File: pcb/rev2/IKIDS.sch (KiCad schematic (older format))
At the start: 41 parts, among them SW1 SW_Push, U1 ATmega32U4-AU, Y1 16MHz

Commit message: Added finished PCB to repo
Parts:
- removed F1: 500mA, Fuse:Fuse_1206_3216Metric, symbol Device:Polyfuse
- removed USB1: Molex-0548190519, random-keyboard-parts:Molex-0548190589, symbol random-keyboard-parts:Molex-0548190519
- removed USB?: HRO-TYPE-C-31-M-12, symbol keebio:HRO-TYPE-C-31-M-12
- added F1: 500mA, Fuse:Fuse_1206_3216Metric, symbol Device:Polyfuse_Small
- added USB1: Molex-0548190589, random-keyboard-parts:Molex-0548190589, symbol random-keyboard-parts:Molex-0548190589
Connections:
- net +5V: now also F1.1
- net D+: now also USB1.3 (D+)
- net D-: now also USB1.4 (D-)
- net GND: now also USB1.1 (GND)
- net VCC: now also F1.2, USB1.5 (VBUS)
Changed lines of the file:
@@
 Comment4 ""
 $EndDescr
-$Comp
-L MCU_Microchip_ATmega:ATmega32U4-AU U1
-U 1 1 607794AF
-P 9540 3080
-F 0 "U1" H 9540 1191 50  0000 C CNN
-F 1 "ATmega32U4-AU" H 9540 1100 50  0000 C CNN
-F 2 "Package_QFP:TQFP-44_10x10mm_P0.8mm" H 9540 3080 50  0001 C CIN
-F 3 "http://ww1.microchip.com/downloads/en/DeviceDoc/Atmel-7766-8-bit-AVR-ATmega16U4-32U4_Datasheet.pdf" H 9540 3080 50  0001 C CNN
-	1    9540 3080
-	1    0    0    -1
-$EndComp
-Wire Wire Line
-	9440 1280 9540 1280
-Connection ~ 9540 1280
-Wire Wire Line
-	9540 1280 9640 1280
 Wire Wire Line
 	9440 1280 9440 1180
-Connection ~ 9440 1280
 $Comp
 L power:+5V #PWR0101
@@
 	1    0    0    -1
 $EndComp
-Wire Wire Line
-	9540 4880 9440 4880
-Connection ~ 9440 4880
-Wire Wire Line
-	9440 4880 9340 4880
 $Comp
 L power:GND #PWR0102
@@
 	1    0    0    -1
 $EndComp
-$Comp
-L random-keyboard-parts:Molex-0548190519 USB1
-U 1 1 6077A7AA
-P 9290 5710
-F 0 "USB1" V 9827 5677 60  0000 C CNN
-F 1 "Molex-0548190519" V 9721 5677 60  0000 C CNN
-F 2 "random-keyboard-parts:Molex-0548190589" H 9290 5710 60  0001 C CNN
-F 3 "" H 9290 5710 60  0001 C CNN
-	1    9290 5710
-	0    -1   -1   0
-$EndComp
-Wire Wire Line
-	9590 5510 9790 5510
-$Comp
-L power:VCC #PWR0111
-U 1 1 6077D28D
-P 9790 5510
-F 0 "#PWR0111" H 9790 5360 50  0001 C CNN
-F 1 "VCC" H 9805 5683 50  0000 C CNN
-F 2 "" H 9790 5510 50  0001 C CNN
-F 3 "" H 9790 5510 50  0001 C CNN
-	1    9790 5510
-	1    0    0    -1
-$EndComp
-Wire Wire Line
-	9790 5510 9990 5510
-Connection ~ 9790 5510
-$Comp
-L Device:Polyfuse F1
-U 1 1 6077E43E
-P 10140 5510
-F 0 "F1" V 9915 5510 50  0000 C CNN
-F 1 "500mA" V 10006 5510 50  0000 C CNN
-F 2 "Fuse:Fuse_1206_3216Metric" H 10190 5310 50  0001 L CNN
-F 3 "~" H 10140 5510 50  0001 C CNN
-	1    10140 5510
-	0    1    1    0
-$EndComp
-Wire Wire Line
-	10290 5510 10390 5510
-$Comp
-L power:+5V #PWR0112
-U 1 1 6077F79A
-P 10390 5510
-F 0 "#PWR0112" H 10390 5360 50  0001 C CNN
-F 1 "+5V" H 10405 5683 50  0000 C CNN
-F 2 "" H 10390 5510 50  0001 C CNN
-F 3 "" H 10390 5510 50  0001 C CNN
-	1    10390 5510
-	1    0    0    -1
-$EndComp
-Text GLabel 9590 5610 2    50   Input ~ 0
-D-
-Text GLabel 9590 5710 2    50   Input ~ 0
-D+
 $Comp
 L MX_Alps_Hybrid:MX-LED MX3
@@
 Text GLabel 3950 3570 3    50   Input ~ 0
 led8
-$Comp
-L keebio:HRO-TYPE-C-31-M-12 USB?
-U 1 1 607E2252
-P 7470 5430
-F 0 "USB?" H 7303 6227 60  0000 C CNN
-F 1 "HRO-TYPE-C-31-M-12" H 7303 6121 60  0000 C CNN
-F 2 "" H 7470 5430 60  0001 C CNN
-F 3 "" H 7470 5430 60  0001 C CNN
-	1    7470 5430
-	1    0    0    -1
-$EndComp
-Wire Wire Line
-	7570 4980 7670 4980
-$Comp
-L power:+5V #PWR?
-U 1 1 607E72D0
-P 7670 4980
-F 0 "#PWR?" H 7670 4830 50  0001 C CNN
-F 1 "+5V" H 7685 5153 50  0000 C CNN
-F 2 "" H 7670 4980 50  0001 C CNN
-F 3 "" H 7670 4980 50  0001 C CNN
-	1    7670 4980
-	1    0    0    -1
-$EndComp
-Wire Wire Line
-	7570 5880 7670 5880
-$Comp
-L power:+5V #PWR?
-U 1 1 607EA54B
-P 7670 5880
-F 0 "#PWR?" H 7670 5730 50  0001 C CNN
-F 1 "+5V" H 7685 6053 50  0000 C CNN
-F 2 "" H 7670 5880 50  0001 C CNN
-F 3 "" H 7670 5880 50  0001 C CNN
-	1    7670 5880
-	1    0    0    -1
-$EndComp
-Wire Wire Line
-	7570 5980 7670 5980
-$Comp
-L power:GND #PWR?
-U 1 1 607EE216
-P 7670 5980
-F 0 "#PWR?" H 7670 5730 50  0001 C CNN
-F 1 "GND" H 7675 5807 50  0000 C CNN
-F 2 "" H 7670 5980 50  0001 C CNN
-F 3 "" H 7670 5980 50  0001 C CNN
-	1    7670 5980
-	1    0    0    -1
-$EndComp
+Connection ~ 9440 4880
+Wire Wire Line
+	9440 4880 9340 4880
+Wire Wire Line
+	9540 4880 9440 4880
+Connection ~ 9440 1280
+Connection ~ 9540 1280
+Wire Wire Line
+	9540 1280 9640 1280
+Wire Wire Line
+	9440 1280 9540 1280
+$Comp
+L MCU_Microchip_ATmega:ATmega32U4-AU U1
+U 1 1 607794AF
+P 9540 3080
+F 0 "U1" H 9540 1191 50  0000 C CNN
+F 1 "ATmega32U4-AU" H 9540 1100 50  0000 C CNN
+F 2 "Package_QFP:TQFP-44_10x10mm_P0.8mm" H 9540 3080 50  0001 C CIN
+F 3 "http://ww1.microchip.com/downloads/en/DeviceDoc/Atmel-7766-8-bit-AVR-ATmega16U4-32U4_Datasheet.pdf" H 9540 3080 50  0001 C CNN
+	1    9540 3080
+	1    0    0    -1
+$EndComp
+$Comp
+L random-keyboard-parts:Molex-0548190589 USB1
+U 1 1 6079F11B
+P 1670 6340
+F 0 "USB1" V 2207 6307 60  0000 C CNN
+F 1 "Molex-0548190589" V 2101 6307 60  0000 C CNN
+F 2 "random-keyboard-parts:Molex-0548190589" H 1670 6340 60  0001 C CNN
+F 3 "" H 1670 6340 60  0001 C CNN
+	1    1670 6340
+	0    -1   -1   0
+$EndComp
+Wire Wire Line
+	1970 6140 2170 6140
+$Comp
+L power:VCC #PWR0111
+U 1 1 607A247B
+P 2170 6140
+F 0 "#PWR0111" H 2170 5990 50  0001 C CNN
+F 1 "VCC" H 2185 6313 50  0000 C CNN
+F 2 "" H 2170 6140 50  0001 C CNN
+F 3 "" H 2170 6140 50  0001 C CNN
+	1    2170 6140
+	1    0    0    -1
+$EndComp
+Wire Wire Line
+	2170 6140 2320 6140
+Connection ~ 2170 6140
+$Comp
+L Device:Polyfuse_Small F1
+U 1 1 607A5C52
+P 2420 6140
+F 0 "F1" V 2215 6140 50  0000 C CNN
+F 1 "500mA" V 2306 6140 50  0000 C CNN
+F 2 "Fuse:Fuse_1206_3216Metric" H 2470 5940 50  0001 L CNN
+F 3 "~" H 2420 6140 50  0001 C CNN
+	1    2420 6140
+	0    1    1    0
+$EndComp
+Wire Wire Line
+	2520 6140 2720 6140
+$Comp
+L power:+5V #PWR0112
+U 1 1 607A8D6A
+P 2720 6140
+F 0 "#PWR0112" H 2720 5990 50  0001 C CNN
+F 1 "+5V" H 2735 6313 50  0000 C CNN
+F 2 "" H 2720 6140 50  0001 C CNN
+F 3 "" H 2720 6140 50  0001 C CNN
+	1    2720 6140
+	1    0    0    -1
+$EndComp
+$Comp
+L power:GND #PWR0122
+U 1 1 607A956C
+P 1970 6540
+F 0 "#PWR0122" H 1970 6290 50  0001 C CNN
+F 1 "GND" H 1975 6367 50  0000 C CNN
+F 2 "" H 1970 6540 50  0001 C CNN
+F 3 "" H 1970 6540 50  0001 C CNN
+	1    1970 6540
+	1    0    0    -1
+$EndComp
+Text GLabel 1970 6240 2    50   Input ~ 0
+D-
+Text GLabel 1970 6340 2    50   Input ~ 0
+D+
 $EndSCHEMATC

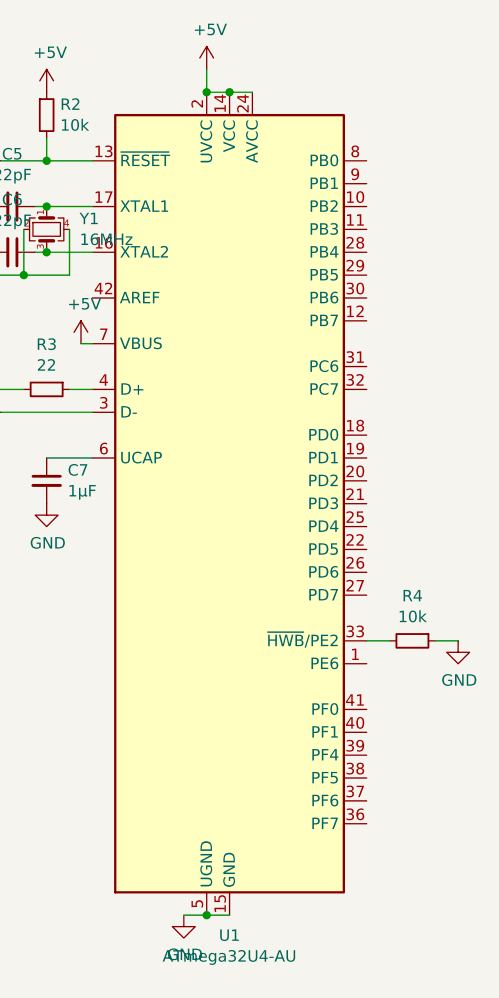
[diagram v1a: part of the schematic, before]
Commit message: added PCB files that doesn't require elite-c
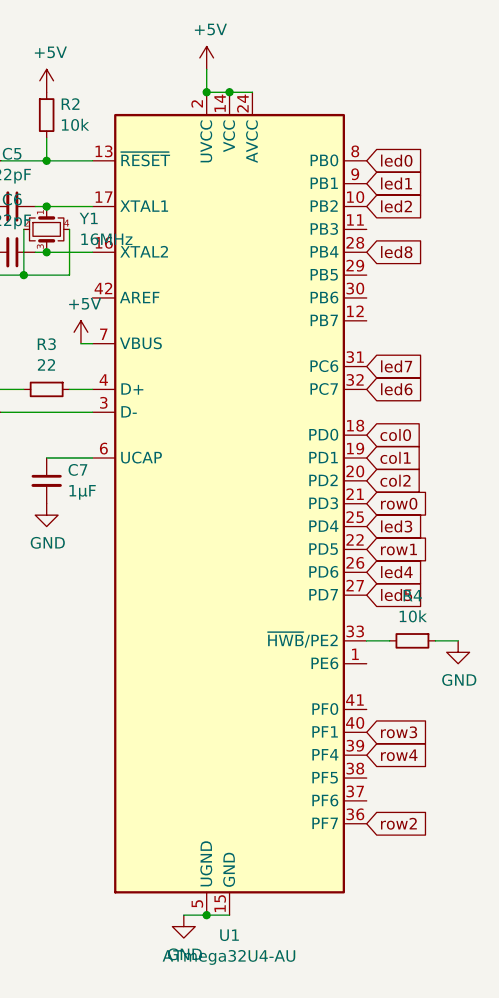
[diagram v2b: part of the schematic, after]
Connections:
- net col0: now also U1.18 (PD0)
- net col1: now also U1.19 (PD1)
- net col2: now also U1.20 (PD2)
- net led0: now also U1.8 (PB0)
- net led1: now also U1.9 (PB1)
- net led2: now also U1.10 (PB2)
- net led3: now also U1.25 (PD4)
- net led4: now also U1.26 (PD6)
- net led5: now also U1.27 (PD7)
- net led6: now also U1.32 (PC7)
- net led7: now also U1.31 (PC6)
- net led8: now also U1.28 (PB4)
- net row0: now also U1.21 (PD3)
- net row1: now also U1.22 (PD5)
- net row2: now also U1.36 (PF7)
- net row3: now also U1.40 (PF1)
- net row4: now also U1.39 (PF4)
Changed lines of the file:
@@
 Text GLabel 1970 6340 2    50   Input ~ 0
 D+
+Text GLabel 10140 2780 2    50   Input ~ 0
+col0
+Text GLabel 10140 2880 2    50   Input ~ 0
+col1
+Text GLabel 10140 2980 2    50   Input ~ 0
+col2
+Text GLabel 10140 3080 2    50   Input ~ 0
+row0
+Text GLabel 10140 3280 2    50   Input ~ 0
+row1
+Text GLabel 10140 4480 2    50   Input ~ 0
+row2
+Text GLabel 10140 1580 2    50   Input ~ 0
+led0
+Text GLabel 10140 1680 2    50   Input ~ 0
+led1
+Text GLabel 10140 1780 2    50   Input ~ 0
+led2
+Text GLabel 10140 3180 2    50   Input ~ 0
+led3
+Text GLabel 10140 3380 2    50   Input ~ 0
+led4
+Text GLabel 10140 3480 2    50   Input ~ 0
+led5
+Text GLabel 10140 2580 2    50   Input ~ 0
+led6
+Text GLabel 10140 2480 2    50   Input ~ 0
+led7
+Text GLabel 10140 1980 2    50   Input ~ 0
+led8
+Text GLabel 10140 4080 2    50   Input ~ 0
+row3
+Text GLabel 10140 4180 2    50   Input ~ 0
+row4
 $EndSCHEMATC
